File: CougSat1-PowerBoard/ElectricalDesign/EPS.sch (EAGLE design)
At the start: 250 parts, among them J1 PV0, J2 PV1, J3 PV2, J4 PV3, J5 Umbilical, J6 SWD, J7 CougSat Card, J8 Deployables, Q1 NTLUD3A50PZ, Q10 DMN2008LFU, Q11 DMN2008LFU, Q12 CSD25402Q3A, Q13 CSD25402Q3A, Q14 NTLUD3A50PZ, Q15 NTLUD3A50PZ, Q16 NTLUD3A50PZ, Q17 NTLUD3A50PZ, Q18 NTLUD3A50PZ, Q19 NTLUD3A50PZ, Q2 NTLUD3A50PZ, Q20 NTLUD3A50PZ, Q21 NTLUD3A50PZ, Q22 NTLUD3A50PZ, Q23 CSD25402Q3A, Q24 CSD25402Q3A, Q25 DMN53D0L, Q26 NTLUD3A50PZ, Q27 NTLUD3A50PZ, Q28 NTLUD3A50PZ, Q29 NTLUD3A50PZ, Q3 NTLUD3A50PZ, Q30 NTLUD3A50PZ, Q31 NTLUD3A50PZ, Q32 NTLUD3A50PZ, Q33 NTLUD3A50PZ, Q34 NTLUD3A50PZ, Q35 NTLUD3A50PZ, Q36 NTLUD3A50PZ, Q37 NTLUD3A50PZ, Q38 NTLUD3A50PZ, Q39 NTLUD3A50PZ, Q4 NTLUD3A50PZ, Q40 NTLUD3A50PZ, Q41 NTLUD3A50PZ, Q42 NTLUD3A50PZ, Q43 NTLUD3A50PZ, Q5 NTLUD3A50PZ, Q6 NTLUD3A50PZ, Q7 NTLUD3A50PZ, Q8 NTLUD3A50PZ, Q9 NTLUD3A50PZ, SW1 D2MQ-1-TL, U1 BQ29700, U10 LTC2499, U11 LTC2499, U12 LTC2499, U13 LTC2499, U14 MCP1501-18, U15 LTC2499, U2 BQ29700, U3 TPS64200, U4 TPS64200, U5 STM32L476RGT, U6 TCA9535R, U7 SN74LVC244AR, U8 TCA9535R, U9 LTC2499

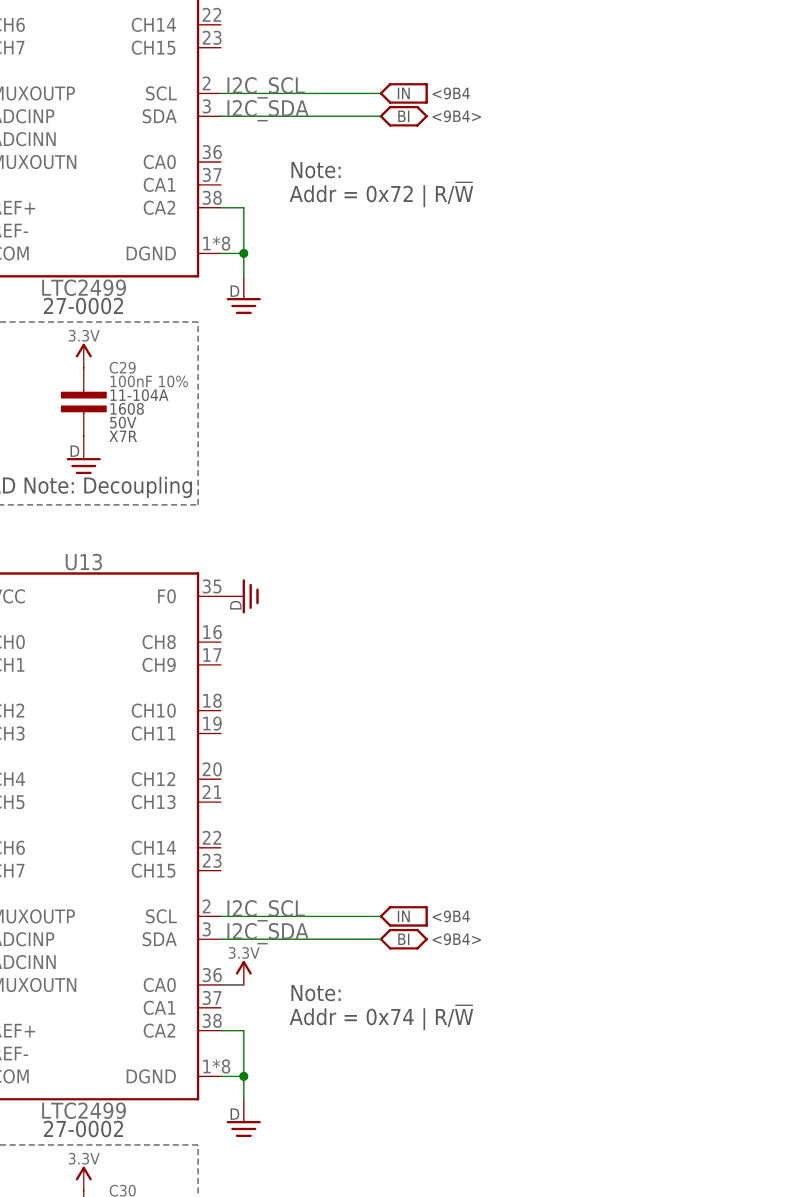
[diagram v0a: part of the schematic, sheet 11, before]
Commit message: Updated I²C Addresses
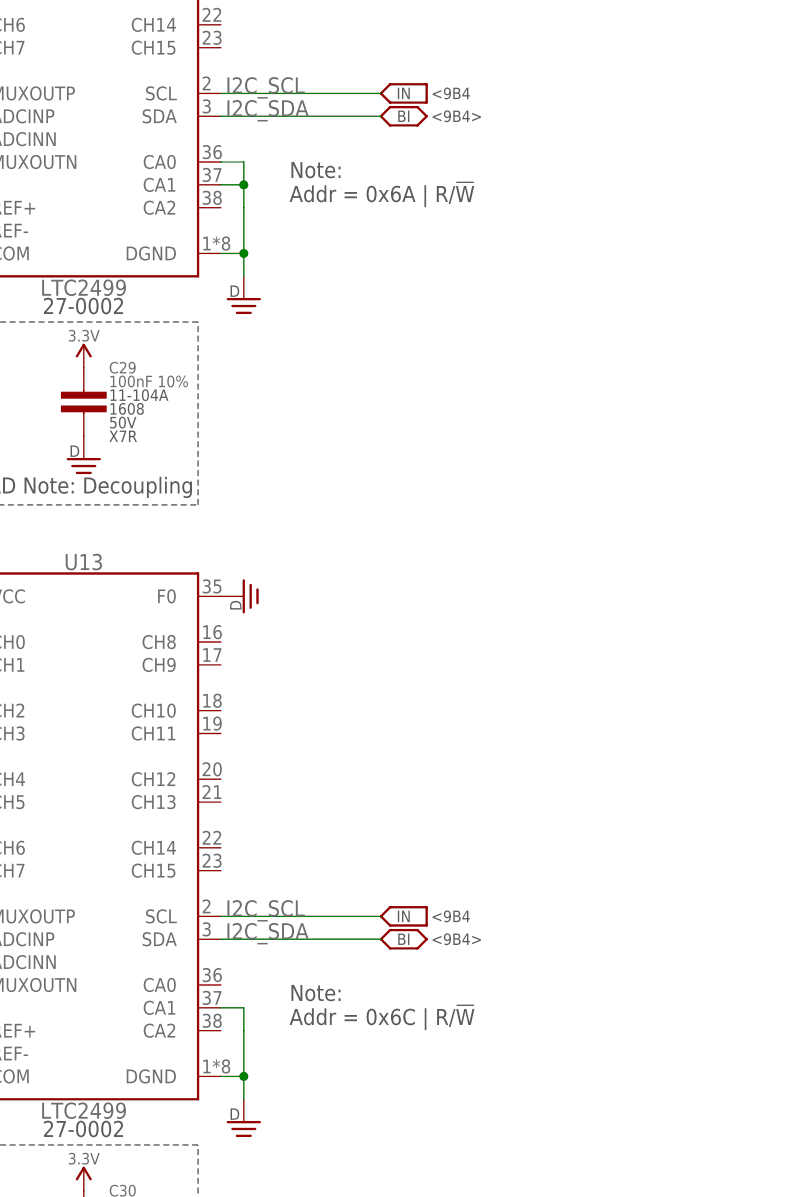
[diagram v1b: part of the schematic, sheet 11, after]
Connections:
- net 3.3V: no longer U13.CA0
- net DGND: now also U12.CA0, U12.CA1, U13.CA1; no longer U12.CA2, U13.CA2
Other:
- note added: "Note: Addr = 0x6A | R/!W"
- note added: "Note: Addr = 0x6C | R/!W"
- note removed: "Note: Addr = 0x72 | R/!W"
- note removed: "Note: Addr = 0x74 | R/!W"

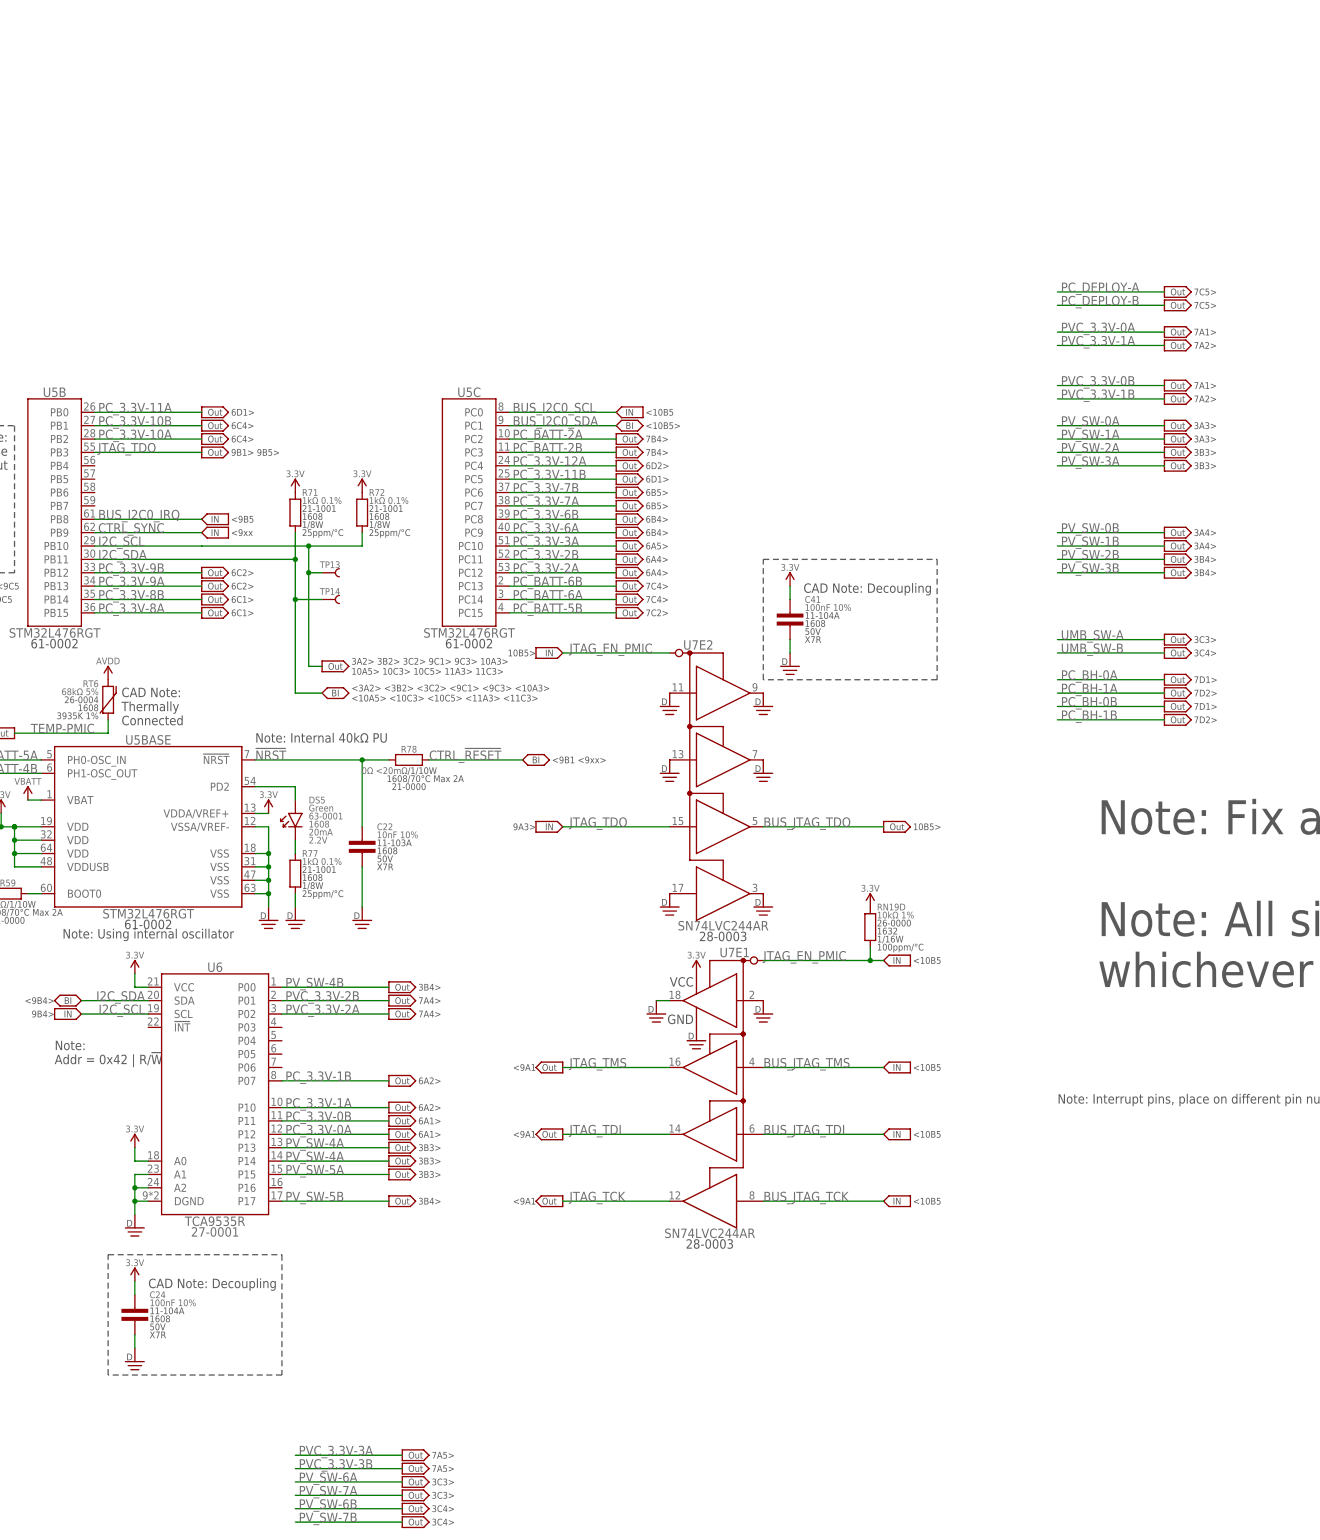
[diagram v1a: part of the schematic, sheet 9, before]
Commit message: Laid Out Voltage ADC
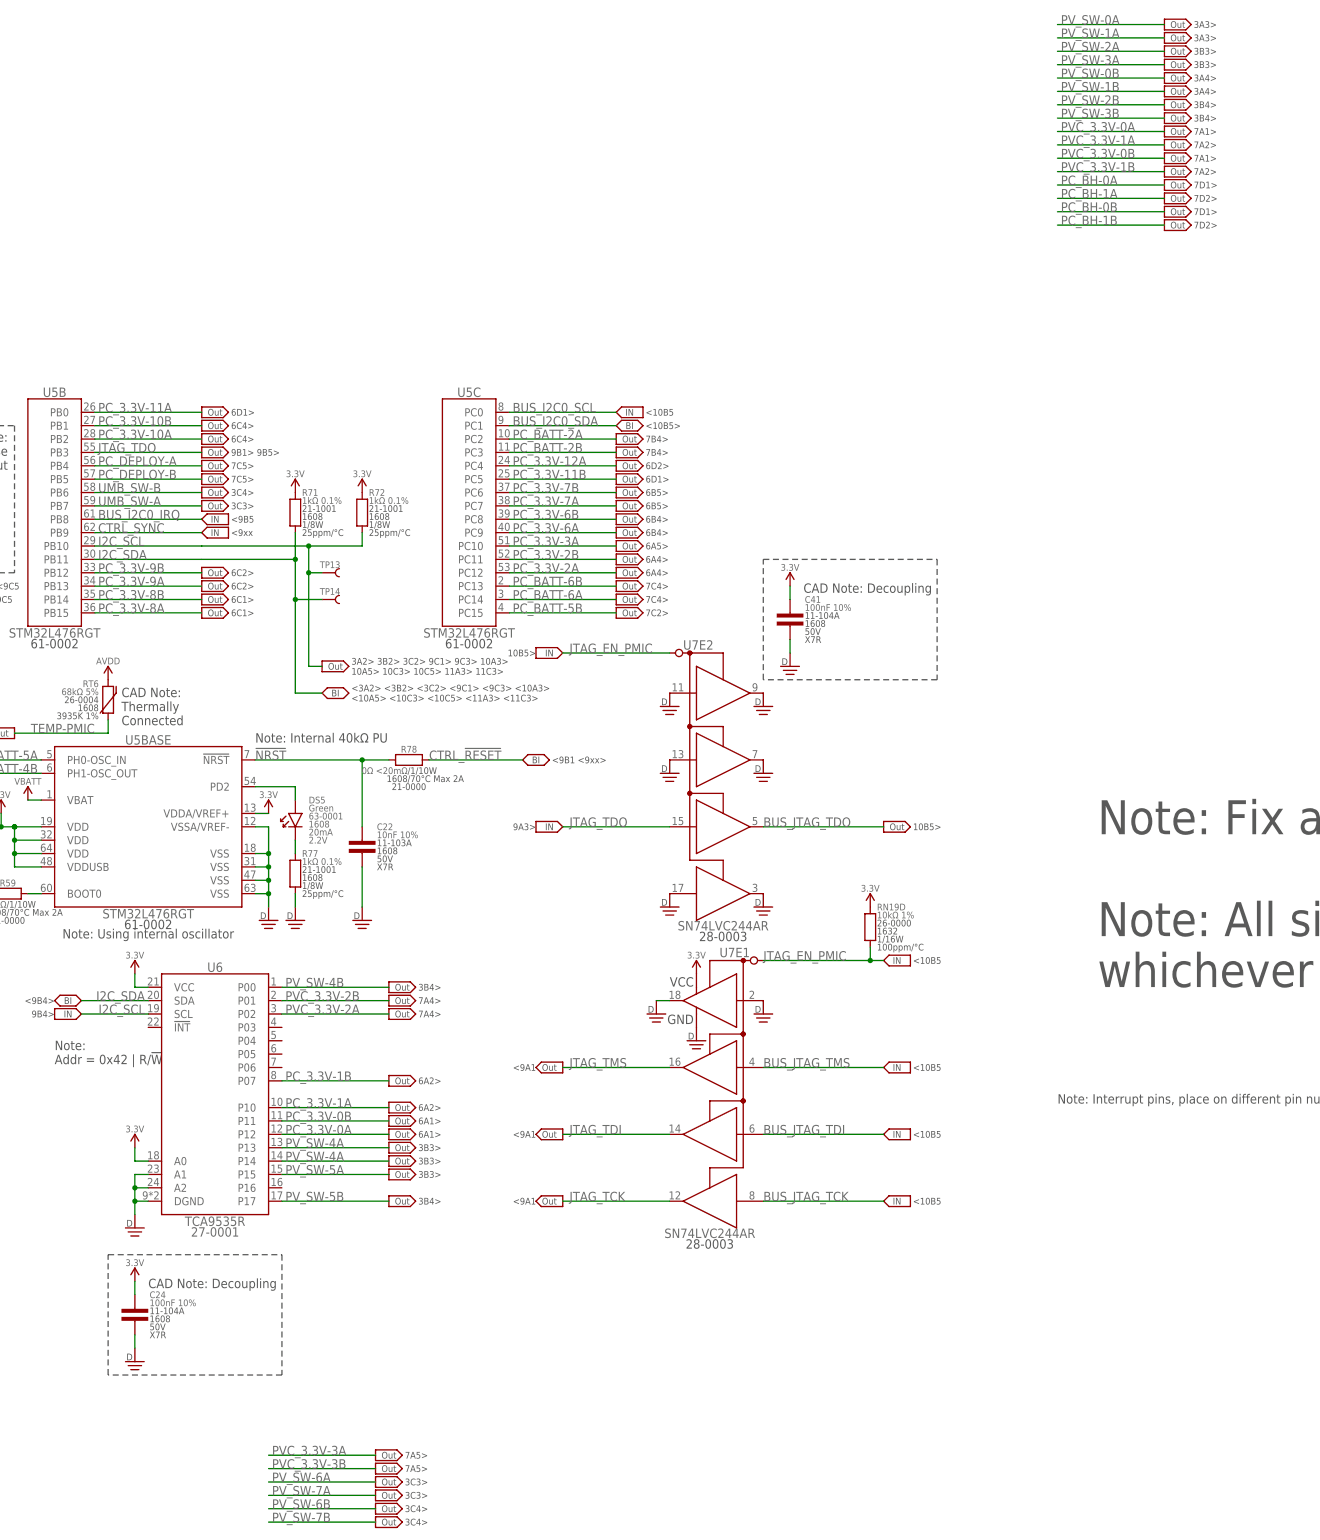
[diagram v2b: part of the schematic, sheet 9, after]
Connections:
- net 3.3V-A: now also U13.CH13
- net 3.3V-B: now also U13.CH14
- net AVREF: now also U13.CH1
- net EJECT_TIMER: now also U13.CH8
- net PC_DEPLOY-A: now also U5B.PB4
- net PC_DEPLOY-B: now also U5B.PB5
- net TEMP+X+Y: now also U13.CH2
- net TEMP+X-Y: now also U13.CH9
- net TEMP-BATT-A: now also U13.CH0
- net TEMP-BATT-B: now also U13.CH11
- net TEMP-PMIC: now also U13.CH4
- net TEMP-REG-A: now also U13.CH6
- net TEMP-REG-B: now also U13.CH15
- net TEMP-X+Y: now also U13.CH5
- net TEMP-X-Y: now also U13.CH10
- net UMB_IN: now also U13.CH3
- net UMB_SW-A: now also U5B.PB7
- net UMB_SW-B: now also U5B.PB6
- net VBATT-A: now also U13.CH7
- net VBATT-B: now also U13.CH12
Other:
- note added: "CAD Note: Place in the corner of the PCB that matches the connected signal name, bottom side"
- note removed: "CAD Note: Place in the corner of the PCB that matches the connected signal name, top side"
